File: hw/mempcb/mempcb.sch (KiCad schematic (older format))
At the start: 26 parts, among them J1 RC6502_Bus, J2 0.1\" 2x25, U3 JEDEC_DIP32_RAM, U4 74LS138

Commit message: hw/mempcb/: assigned footprints
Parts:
- BUSPWR_EN: value JST-XH -> 0.1\" 1x2; footprint (none) -> Connector_PinHeader_2.54mm:PinHeader_1x02_P2.54mm_Vertical
- HIGH, LOW, PULLDOWN, PULLUP: footprint (none) -> Connector_PinHeader_2.54mm:PinHeader_1x04_P2.54mm_Vertical
- J1: footprint (none) -> Connector_PinHeader_2.54mm:PinHeader_1x39_P2.54mm_Horizontal
- J2: footprint (none) -> Connector_PinHeader_2.54mm:PinHeader_2x25_P2.54mm_Vertical
- PWR1, PWR2: footprint (none) -> Connector_JST:JST_XH_B2B-XH-A_1x02_P2.50mm_Vertical
- R1, R2, R3, R4, R5, R6, R7, R8: footprint (none) -> Resistor_THT:R_Axial_DIN0207_L6.3mm_D2.5mm_P10.16mm_Horizontal
- U3: footprint (none) -> Package_DIP:DIP-32_W15.24mm_Socket_LongPads
- U4: footprint (none) -> Package_DIP:DIP-16_W7.62mm_Socket_LongPads
- W1: footprint (none) -> Connector_PinHeader_2.54mm:PinHeader_1x39_P2.54mm_Vertical
- W2A, W2B: footprint (none) -> Connector_PinHeader_2.54mm:PinHeader_1x25_P2.54mm_Vertical
- W3A, W3B: footprint (none) -> Connector_PinHeader_2.54mm:PinHeader_1x16_P2.54mm_Vertical
- W4A, W4B: footprint (none) -> Connector_PinHeader_2.54mm:PinHeader_1x08_P2.54mm_Vertical
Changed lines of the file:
@@
 F 0 "J1" H 2000 4950 50  0000 C CNN
 F 1 "RC6502_Bus" H 1958 4890 50  0001 C CNN
-F 2 "" H 1850 2900 50  0001 C CNN
+F 2 "Connector_PinHeader_2.54mm:PinHeader_1x39_P2.54mm_Horizontal" H 1850 2900 50  0001 C CNN
 F 3 "~" H 1850 2900 50  0001 C CNN
 	1    1850 2900
@@
 F 0 "W1" H 2850 4950 50  0000 R CNN
 F 1 "RC6502_Bus" H 2300 4850 50  0001 R CNN
-F 2 "" H 2700 2900 50  0001 C CNN
+F 2 "Connector_PinHeader_2.54mm:PinHeader_1x39_P2.54mm_Vertical" H 2700 2900 50  0001 C CNN
 F 3 "~" H 2700 2900 50  0001 C CNN
 	1    2700 2900
@@
 F 0 "U3" H 5500 3267 50  0000 C CNN
 F 1 "JEDEC_DIP32_RAM" H 5500 3176 50  0000 C CNN
-F 2 "" H 5500 2100 50  0001 C CNN
+F 2 "Package_DIP:DIP-32_W15.24mm_Socket_LongPads" H 5500 2100 50  0001 C CNN
 F 3 "http://www.futurlec.com/Datasheet/Memory/628128.pdf" H 5500 2100 50  0001 C CNN
 	1    5500 2100
@@
 F 0 "J2" H 8900 4200 50  0000 C CNN
 F 1 "0.1\" 2x25" H 8900 4100 50  0000 C CNN
-F 2 "" H 8850 2750 50  0001 C CNN
+F 2 "Connector_PinHeader_2.54mm:PinHeader_2x25_P2.54mm_Vertical" H 8850 2750 50  0001 C CNN
 F 3 "~" H 8850 2750 50  0001 C CNN
 	1    8850 2750
@@
 F 0 "W2A" H 8250 4200 50  0000 C CNN
 F 1 "0.1\" 1x25" H 8250 4100 50  0000 C CNN
-F 2 "" H 8250 2750 50  0001 C CNN
+F 2 "Connector_PinHeader_2.54mm:PinHeader_1x25_P2.54mm_Vertical" H 8250 2750 50  0001 C CNN
 F 3 "~" H 8250 2750 50  0001 C CNN
 	1    8250 2750
@@
 F 0 "W2B" H 9450 4200 50  0000 L CNN
 F 1 "0.1\" 1x25" H 9350 4100 50  0000 L CNN
-F 2 "" H 9550 2750 50  0001 C CNN
+F 2 "Connector_PinHeader_2.54mm:PinHeader_1x25_P2.54mm_Vertical" H 9550 2750 50  0001 C CNN
 F 3 "~" H 9550 2750 50  0001 C CNN
 	1    9550 2750
@@
 F 0 "W3A" H 4550 2950 50  0000 C CNN
 F 1 "0.1\" 1x16" H 4468 2826 50  0000 C CNN
-F 2 "" H 4550 2000 50  0001 C CNN
+F 2 "Connector_PinHeader_2.54mm:PinHeader_1x16_P2.54mm_Vertical" H 4550 2000 50  0001 C CNN
 F 3 "~" H 4550 2000 50  0001 C CNN
 	1    4550 2000
@@
 F 0 "W4B" H 6400 4650 50  0000 L CNN
 F 1 "0.1\" 1x8" H 6350 4550 50  0000 L CNN
-F 2 "" H 6500 4100 50  0001 C CNN
+F 2 "Connector_PinHeader_2.54mm:PinHeader_1x08_P2.54mm_Vertical" H 6500 4100 50  0001 C CNN
 F 3 "~" H 6500 4100 50  0001 C CNN
 	1    6500 4100
@@
 F 0 "W4A" H 4418 4617 50  0000 C CNN
 F 1 "0.1\" 1x8" H 4418 4526 50  0000 C CNN
-F 2 "" H 4500 4100 50  0001 C CNN
+F 2 "Connector_PinHeader_2.54mm:PinHeader_1x08_P2.54mm_Vertical" H 4500 4100 50  0001 C CNN
 F 3 "~" H 4500 4100 50  0001 C CNN
 	1    4500 4100
@@
 F 0 "W3B" H 6350 2950 50  0000 L CNN
 F 1 "0.1\" 1x16" H 6250 2850 50  0000 L CNN
-F 2 "" H 6450 2000 50  0001 C CNN
+F 2 "Connector_PinHeader_2.54mm:PinHeader_1x16_P2.54mm_Vertical" H 6450 2000 50  0001 C CNN
 F 3 "~" H 6450 2000 50  0001 C CNN
 	1    6450 2000
@@
 F 0 "U4" H 5500 4667 50  0000 C CNN
 F 1 "74LS138" H 5500 4576 50  0000 C CNN
-F 2 "" H 5500 4100 50  0001 C CNN
+F 2 "Package_DIP:DIP-16_W7.62mm_Socket_LongPads" H 5500 4100 50  0001 C CNN
 F 3 "http://www.ti.com/lit/gpn/sn74LS138" H 5500 4100 50  0001 C CNN
 	1    5500 4100
@@
 F 0 "HIGH" V 4050 5950 50  0000 R CNN
 F 1 "0.1\" 1x4" V 3950 6000 50  0000 R CNN
-F 2 "" H 3850 5900 50  0001 C CNN
+F 2 "Connector_PinHeader_2.54mm:PinHeader_1x04_P2.54mm_Vertical" H 3850 5900 50  0001 C CNN
 F 3 "~" H 3850 5900 50  0001 C CNN
 	1    3850 5900
@@
 F 0 "LOW" V 4600 5950 50  0000 R CNN
 F 1 "0.1\" 1x4" V 4500 6000 50  0000 R CNN
-F 2 "" H 4400 5900 50  0001 C CNN
+F 2 "Connector_PinHeader_2.54mm:PinHeader_1x04_P2.54mm_Vertical" H 4400 5900 50  0001 C CNN
 F 3 "~" H 4400 5900 50  0001 C CNN
 	1    4400 5900
@@
 F 0 "PULLUP" V 3550 6000 50  0000 R CNN
 F 1 "0.1\" 1x4" V 3450 6000 50  0000 R CNN
-F 2 "" H 3350 5900 50  0001 C CNN
+F 2 "Connector_PinHeader_2.54mm:PinHeader_1x04_P2.54mm_Vertical" H 3350 5900 50  0001 C CNN
 F 3 "~" H 3350 5900 50  0001 C CNN
 	1    3350 5900
@@
 F 0 "R2" V 3350 6350 50  0000 C CNN
 F 1 "R" V 3350 6350 50  0001 C CNN
-F 2 "" V 3280 6350 50  0001 C CNN
+F 2 "Resistor_THT:R_Axial_DIN0207_L6.3mm_D2.5mm_P10.16mm_Horizontal" V 3280 6350 50  0001 C CNN
 F 3 "~" H 3350 6350 50  0001 C CNN
 	1    3350 6350
@@
 F 0 "R3" V 3450 6350 50  0000 C CNN
 F 1 "R" V 3450 6350 50  0001 C CNN
-F 2 "" V 3380 6350 50  0001 C CNN
+F 2 "Resistor_THT:R_Axial_DIN0207_L6.3mm_D2.5mm_P10.16mm_Horizontal" V 3380 6350 50  0001 C CNN
 F 3 "~" H 3450 6350 50  0001 C CNN
 	1    3450 6350
@@
 F 0 "R4" V 3550 6350 50  0000 C CNN
 F 1 "R" V 3550 6350 50  0001 C CNN
-F 2 "" V 3480 6350 50  0001 C CNN
+F 2 "Resistor_THT:R_Axial_DIN0207_L6.3mm_D2.5mm_P10.16mm_Horizontal" V 3480 6350 50  0001 C CNN
 F 3 "~" H 3550 6350 50  0001 C CNN
 	1    3550 6350
@@
 F 0 "PULLDOWN" V 5100 6050 50  0000 R CNN
 F 1 "0.1\" 1x4" V 5000 6000 50  0000 R CNN
-F 2 "" H 4900 5900 50  0001 C CNN
+F 2 "Connector_PinHeader_2.54mm:PinHeader_1x04_P2.54mm_Vertical" H 4900 5900 50  0001 C CNN
 F 3 "~" H 4900 5900 50  0001 C CNN
 	1    4900 5900
@@
 F 0 "R5" V 4800 6350 50  0000 C CNN
 F 1 "R" V 4800 6350 50  0001 C CNN
-F 2 "" V 4730 6350 50  0001 C CNN
+F 2 "Resistor_THT:R_Axial_DIN0207_L6.3mm_D2.5mm_P10.16mm_Horizontal" V 4730 6350 50  0001 C CNN
 F 3 "~" H 4800 6350 50  0001 C CNN
 	1    4800 6350
@@
 F 0 "R6" V 4900 6350 50  0000 C CNN
 F 1 "R" V 4900 6350 50  0001 C CNN
-F 2 "" V 4830 6350 50  0001 C CNN
+F 2 "Resistor_THT:R_Axial_DIN0207_L6.3mm_D2.5mm_P10.16mm_Horizontal" V 4830 6350 50  0001 C CNN
 F 3 "~" H 4900 6350 50  0001 C CNN
 	1    4900 6350
@@
 F 0 "R7" V 5000 6350 50  0000 C CNN
 F 1 "R" V 5000 6350 50  0001 C CNN
-F 2 "" V 4930 6350 50  0001 C CNN
+F 2 "Resistor_THT:R_Axial_DIN0207_L6.3mm_D2.5mm_P10.16mm_Horizontal" V 4930 6350 50  0001 C CNN
 F 3 "~" H 5000 6350 50  0001 C CNN
 	1    5000 6350
@@
 F 0 "R8" V 5100 6350 50  0000 C CNN
 F 1 "R" V 5100 6350 50  0001 C CNN
-F 2 "" V 5030 6350 50  0001 C CNN
+F 2 "Resistor_THT:R_Axial_DIN0207_L6.3mm_D2.5mm_P10.16mm_Horizontal" V 5030 6350 50  0001 C CNN
 F 3 "~" H 5100 6350 50  0001 C CNN
 	1    5100 6350
@@
 F 0 "R1" V 3250 6350 50  0000 C CNN
 F 1 "R" V 3250 6350 50  0001 C CNN
-F 2 "" V 3180 6350 50  0001 C CNN
+F 2 "Resistor_THT:R_Axial_DIN0207_L6.3mm_D2.5mm_P10.16mm_Horizontal" V 3180 6350 50  0001 C CNN
 F 3 "~" H 3250 6350 50  0001 C CNN
 	1    3250 6350
@@
 F 0 "PWR1" H 2750 5900 50  0000 R CNN
 F 1 "JST-XH" H 2800 5800 50  0000 R CNN
-F 2 "" H 2450 5900 50  0001 C CNN
+F 2 "Connector_JST:JST_XH_B2B-XH-A_1x02_P2.50mm_Vertical" H 2450 5900 50  0001 C CNN
 F 3 "~" H 2450 5900 50  0001 C CNN
 	1    2450 5900
@@
 F 0 "PWR2" H 3050 5900 50  0000 R CNN
 F 1 "JST-XH" H 3100 5800 50  0000 R CNN
-F 2 "" H 2750 5900 50  0001 C CNN
+F 2 "Connector_JST:JST_XH_B2B-XH-A_1x02_P2.50mm_Vertical" H 2750 5900 50  0001 C CNN
 F 3 "~" H 2750 5900 50  0001 C CNN
 	1    2750 5900
@@
 P 1900 5900
 F 0 "BUSPWR_EN" H 2400 5900 50  0000 R CNN
-F 1 "JST-XH" H 2250 5800 50  0000 R CNN
-F 2 "" H 1900 5900 50  0001 C CNN
+F 1 "0.1\" 1x2" H 2300 5800 50  0000 R CNN
+F 2 "Connector_PinHeader_2.54mm:PinHeader_1x02_P2.54mm_Vertical" H 1900 5900 50  0001 C CNN
 F 3 "~" H 1900 5900 50  0001 C CNN
 	1    1900 5900

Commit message: hw/mempcb/: fix annotations to end with a number
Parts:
- renumbered BUSPWR_EN to BUSPWR_EN1, HIGH to HIGH1, LOW to LOW1, PULLDOWN to PULLDOWN1, PULLUP to PULLUP1, W2A to W2_1, W2B to W2_2, W3A to W3_1, W3B to W3_2, W4A to W4_1, W4B to W4_2
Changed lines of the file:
@@
 $EndComp
 $Comp
-L Connector_Generic:Conn_01x25 W2A
+L Connector_Generic:Conn_01x25 W2_1
 U 1 1 5FEB2EF1
 P 8250 2750
-F 0 "W2A" H 8250 4200 50  0000 C CNN
+F 0 "W2_1" H 8250 4200 50  0000 C CNN
 F 1 "0.1\" 1x25" H 8250 4100 50  0000 C CNN
 F 2 "Connector_PinHeader_2.54mm:PinHeader_1x25_P2.54mm_Vertical" H 8250 2750 50  0001 C CNN
@@
 $EndComp
 $Comp
-L Connector_Generic:Conn_01x25 W2B
+L Connector_Generic:Conn_01x25 W2_2
 U 1 1 5FEC1F3E
 P 9550 2750
-F 0 "W2B" H 9450 4200 50  0000 L CNN
+F 0 "W2_2" H 9450 4200 50  0000 L CNN
 F 1 "0.1\" 1x25" H 9350 4100 50  0000 L CNN
 F 2 "Connector_PinHeader_2.54mm:PinHeader_1x25_P2.54mm_Vertical" H 9550 2750 50  0001 C CNN
@@
 $EndComp
 $Comp
-L Connector_Generic:Conn_01x16 W3A
+L Connector_Generic:Conn_01x16 W3_1
 U 1 1 5FECEA90
 P 4550 2000
-F 0 "W3A" H 4550 2950 50  0000 C CNN
+F 0 "W3_1" H 4550 2950 50  0000 C CNN
 F 1 "0.1\" 1x16" H 4468 2826 50  0000 C CNN
 F 2 "Connector_PinHeader_2.54mm:PinHeader_1x16_P2.54mm_Vertical" H 4550 2000 50  0001 C CNN
@@
 $EndComp
 $Comp
-L Connector_Generic:Conn_01x08 W4B
+L Connector_Generic:Conn_01x08 W4_2
 U 1 1 5FECFD2E
 P 6500 4100
-F 0 "W4B" H 6400 4650 50  0000 L CNN
+F 0 "W4_2" H 6400 4650 50  0000 L CNN
 F 1 "0.1\" 1x8" H 6350 4550 50  0000 L CNN
 F 2 "Connector_PinHeader_2.54mm:PinHeader_1x08_P2.54mm_Vertical" H 6500 4100 50  0001 C CNN
@@
 $EndComp
 $Comp
-L Connector_Generic:Conn_01x08 W4A
+L Connector_Generic:Conn_01x08 W4_1
 U 1 1 5FED086C
 P 4500 4100
-F 0 "W4A" H 4418 4617 50  0000 C CNN
+F 0 "W4_1" H 4418 4617 50  0000 C CNN
 F 1 "0.1\" 1x8" H 4418 4526 50  0000 C CNN
 F 2 "Connector_PinHeader_2.54mm:PinHeader_1x08_P2.54mm_Vertical" H 4500 4100 50  0001 C CNN
@@
 	6250 1300 6000 1300
 $Comp
-L Connector_Generic:Conn_01x16 W3B
+L Connector_Generic:Conn_01x16 W3_2
 U 1 1 5FECF06C
 P 6450 2000
-F 0 "W3B" H 6350 2950 50  0000 L CNN
+F 0 "W3_2" H 6350 2950 50  0000 L CNN
 F 1 "0.1\" 1x16" H 6250 2850 50  0000 L CNN
 F 2 "Connector_PinHeader_2.54mm:PinHeader_1x16_P2.54mm_Vertical" H 6450 2000 50  0001 C CNN
@@
 VCC
 $Comp
-L Connector_Generic:Conn_01x04 HIGH
+L Connector_Generic:Conn_01x04 HIGH1
 U 1 1 5FED18C8
 P 3850 5900
-F 0 "HIGH" V 4050 5950 50  0000 R CNN
+F 0 "HIGH1" V 4050 5950 50  0000 R CNN
 F 1 "0.1\" 1x4" V 3950 6000 50  0000 R CNN
 F 2 "Connector_PinHeader_2.54mm:PinHeader_1x04_P2.54mm_Vertical" H 3850 5900 50  0001 C CNN
@@
 $EndComp
 $Comp
-L Connector_Generic:Conn_01x04 LOW
+L Connector_Generic:Conn_01x04 LOW1
 U 1 1 603235A5
 P 4400 5900
-F 0 "LOW" V 4600 5950 50  0000 R CNN
+F 0 "LOW1" V 4600 5950 50  0000 R CNN
 F 1 "0.1\" 1x4" V 4500 6000 50  0000 R CNN
 F 2 "Connector_PinHeader_2.54mm:PinHeader_1x04_P2.54mm_Vertical" H 4400 5900 50  0001 C CNN
@@
 $EndComp
 $Comp
-L Connector_Generic:Conn_01x04 PULLUP
+L Connector_Generic:Conn_01x04 PULLUP1
 U 1 1 6032F1DA
 P 3350 5900
-F 0 "PULLUP" V 3550 6000 50  0000 R CNN
+F 0 "PULLUP1" V 3550 6000 50  0000 R CNN
 F 1 "0.1\" 1x4" V 3450 6000 50  0000 R CNN
 F 2 "Connector_PinHeader_2.54mm:PinHeader_1x04_P2.54mm_Vertical" H 3350 5900 50  0001 C CNN
@@
 	3450 6600 3550 6600
 $Comp
-L Connector_Generic:Conn_01x04 PULLDOWN
+L Connector_Generic:Conn_01x04 PULLDOWN1
 U 1 1 6042687B
 P 4900 5900
-F 0 "PULLDOWN" V 5100 6050 50  0000 R CNN
+F 0 "PULLDOWN1" V 5100 6050 50  0000 R CNN
 F 1 "0.1\" 1x4" V 5000 6000 50  0000 R CNN
 F 2 "Connector_PinHeader_2.54mm:PinHeader_1x04_P2.54mm_Vertical" H 4900 5900 50  0001 C CNN
@@
 BUS_VCC
 $Comp
-L Connector_Generic:Conn_01x02 BUSPWR_EN
+L Connector_Generic:Conn_01x02 BUSPWR_EN1
 U 1 1 60556D43
 P 1900 5900
-F 0 "BUSPWR_EN" H 2400 5900 50  0000 R CNN
+F 0 "BUSPWR_EN1" H 2400 5900 50  0000 R CNN
 F 1 "0.1\" 1x2" H 2300 5800 50  0000 R CNN
 F 2 "Connector_PinHeader_2.54mm:PinHeader_1x02_P2.54mm_Vertical" H 1900 5900 50  0001 C CNN

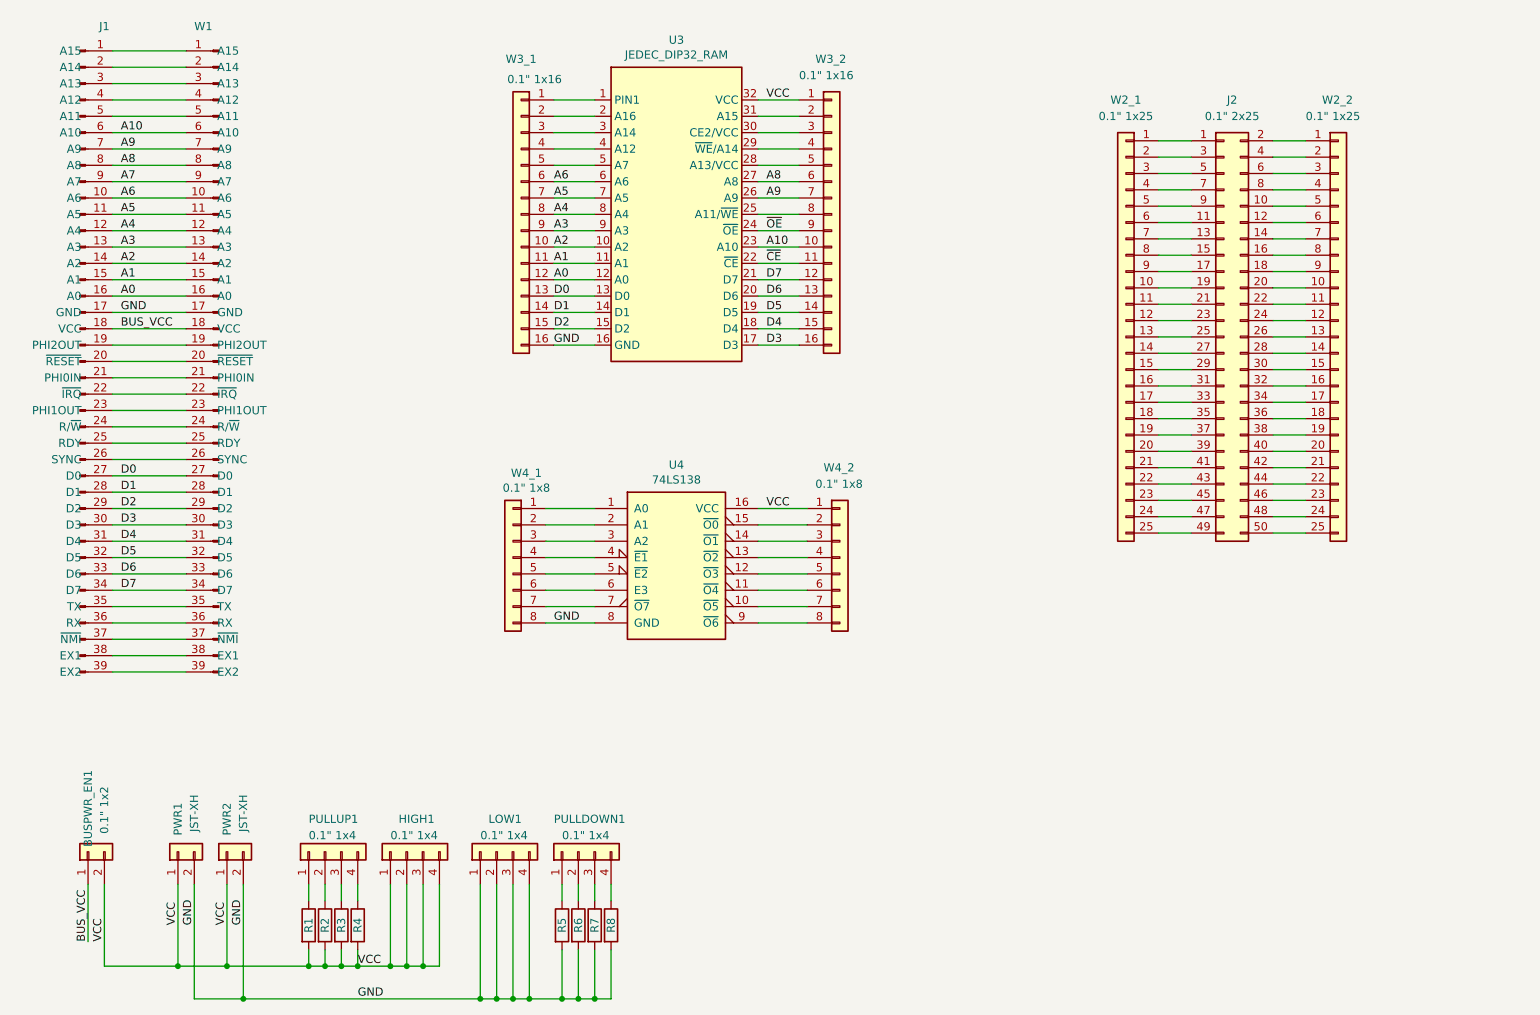
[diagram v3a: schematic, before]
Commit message: BROKEN hw/mempcb/: add another DIP16 and bypass caps
For 6502 systems, qualifying the RAM write line with Φ2 is essential for
reliable operation. If a 74'138 is used for address decoding, we will need
some separate gates for that, so add another socket for those.

The RC6502 bus connector is still backwards.
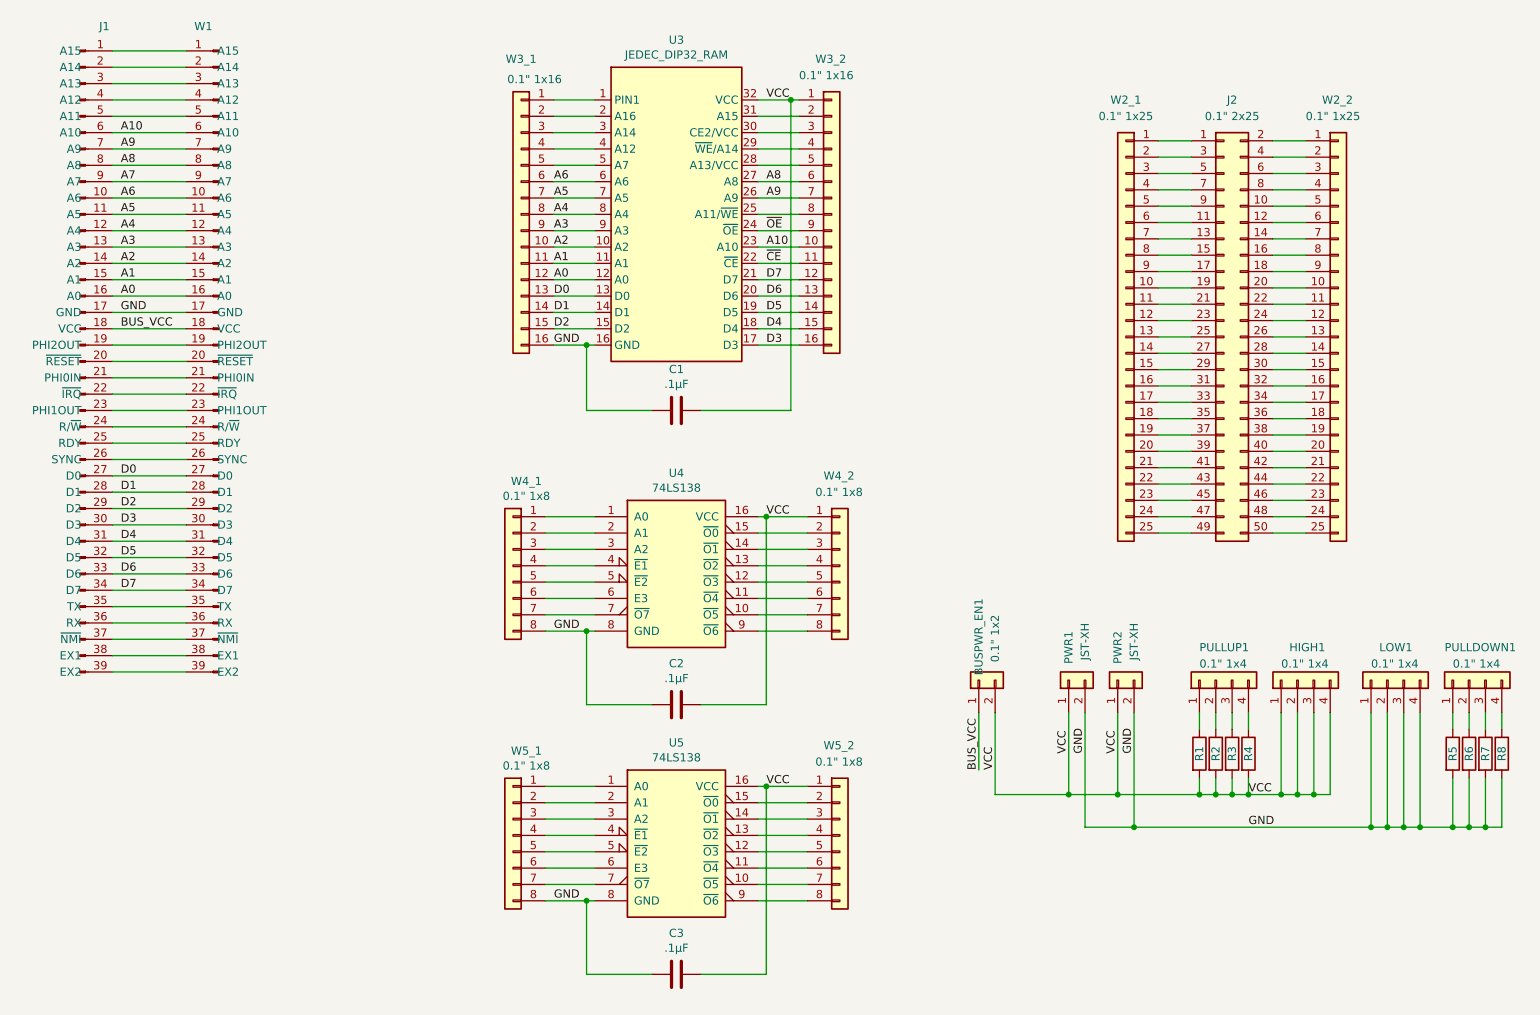
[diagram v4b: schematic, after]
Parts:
- added C1, C2, C3: .1μF, Capacitor_THT:C_Disc_D5.0mm_W2.5mm_P5.00mm, symbol Device:C
- added U5: 74LS138, Package_DIP:DIP-16_W7.62mm_Socket_LongPads, symbol mempcb:74LS138
- added W5_1, W5_2: 0.1\" 1x8, Connector_PinHeader_2.54mm:PinHeader_1x08_P2.54mm_Vertical, symbol Connector_Generic:Conn_01x08
- J1: footprint Connector_PinHeader_2.54mm:PinHeader_1x39_P2.54mm_Horizontal -> Connector_PinHeader_2.54mm:PinHeader_1x39_P2.54mm_Vertical
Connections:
- net GND: now also C1.2, C2.2, C3.2, U5.8 (GND), W5_1.8 (Pin_8)
- net VCC: now also C1.1, C2.1, C3.1, U5.16 (VCC), W5_2.1 (Pin_1)
- new net: U5.15 (~O0), W5_2.2 (Pin_2)
- new net: U5.14 (~O1), W5_2.3 (Pin_3)
- new net: U5.13 (~O2), W5_2.4 (Pin_4)
- new net: U5.12 (~O3), W5_2.5 (Pin_5)
- new net: U5.11 (~O4), W5_2.6 (Pin_6)
- new net: U5.10 (~O5), W5_2.7 (Pin_7)
- new net: U5.9 (~O6), W5_2.8 (Pin_8)
- new net: U5.1 (A0), W5_1.1 (Pin_1)
- new net: U5.2 (A1), W5_1.2 (Pin_2)
- new net: U5.3 (A2), W5_1.3 (Pin_3)
- new net: U5.4 (~E1), W5_1.4 (Pin_4)
- new net: U5.5 (~E2), W5_1.5 (Pin_5)
- new net: U5.6 (E3), W5_1.6 (Pin_6)
- new net: U5.7 (~O7), W5_1.7 (Pin_7)
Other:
- moved on the sheet: BUSPWR_EN1, HIGH1, LOW1, PULLDOWN1, PULLUP1, PWR1, PWR2, R1, R2, R3, R4, R5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
